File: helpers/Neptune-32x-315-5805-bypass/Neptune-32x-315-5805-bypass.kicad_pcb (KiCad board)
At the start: 2 copper layers, 16 x 22 mm, 1 part, among them IC1 315-5805

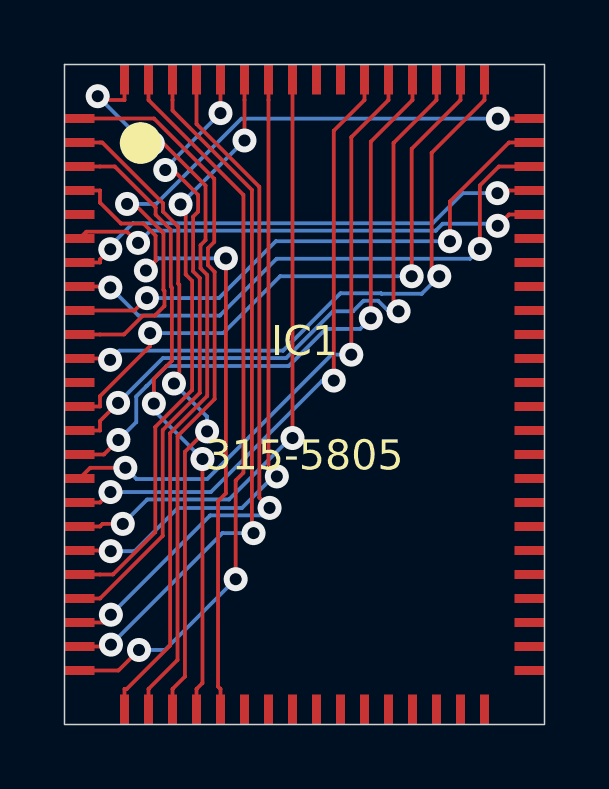
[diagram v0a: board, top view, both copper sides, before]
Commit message: Update bypass flexes for 315-5805 and 315-5818 for better connection (issue #11).
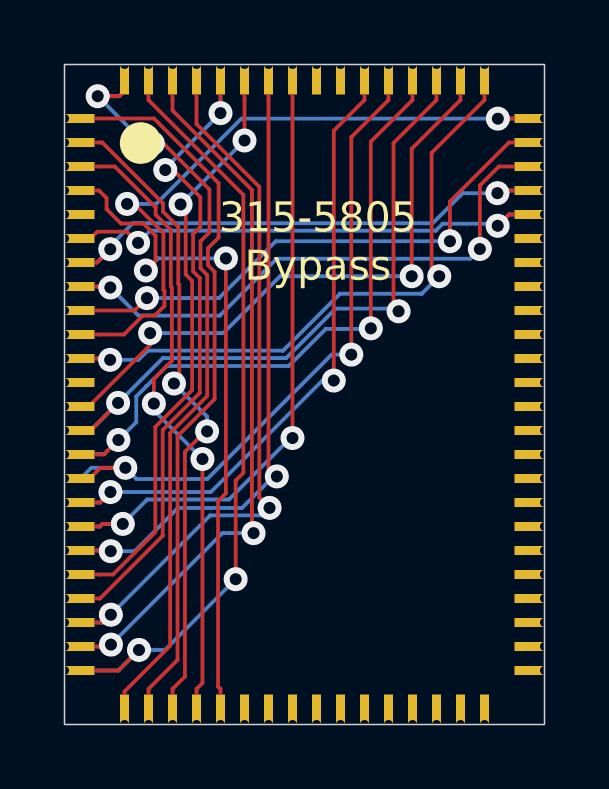
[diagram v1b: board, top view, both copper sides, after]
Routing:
- net VA22: track 16.1 -> 20.4 mm
- net VA6: track 24.5 -> 27.3 mm
- net VA15: track 20.6 -> 22.9 mm
- net VA14: track 20.8 -> 22.9 mm
- net VA12: track 20.3 -> 22.3 mm
- net VA16: track 21.2 -> 22.9 mm
- net VA23: track 15.7 -> 17.4 mm
- net VA9: track 20.9 -> 22.6 mm
- net VA13: track 20.6 -> 22.3 mm
- net VA8: track 23.2 -> 24.9 mm
- net VA5: track 25.3 -> 26.9 mm
- net VA7: track 23.6 -> 25.2 mm
- net VA19: track 21.9 -> 23.4 mm
- net VA11: track 21.0 -> 22.5 mm
- net VA21: track 18.7 -> 20.2 mm
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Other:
- board text added: "315-5805 Bypass"
